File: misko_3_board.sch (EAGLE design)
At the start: 179 parts, among them IC1 ATMEGA1281-16AU, IC10 ORG1510-MK4, IC11 TPS3808G33DBVT, IC12 LTC4425, IC13 RN-42, IC14 ADXL345, IC15 74HCT1G32, IC16 FM25W256-SOIC, IC17 MICROSD_SPI_MODE, IC18 FH12-30S-0.5SH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

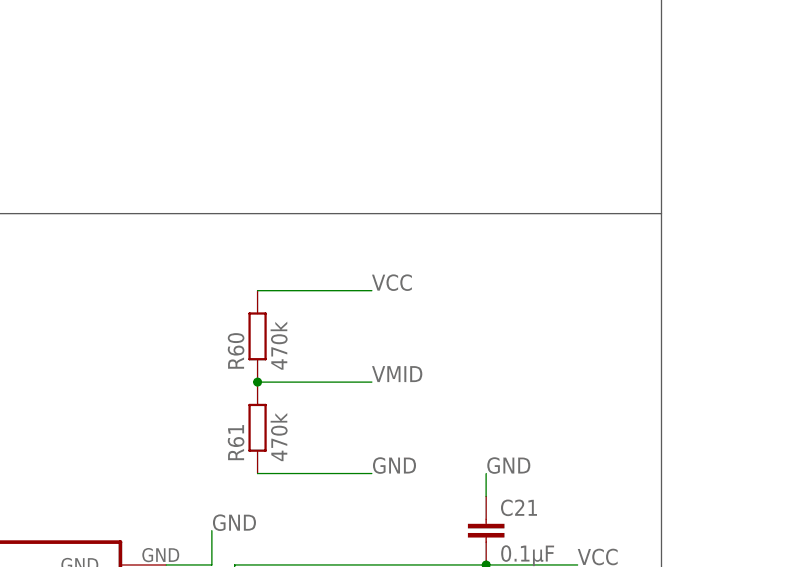
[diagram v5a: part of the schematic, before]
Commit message: - corrected resisitor divider for LTC4425 - R60/61 now connect to Vgps (instead of Vcc)
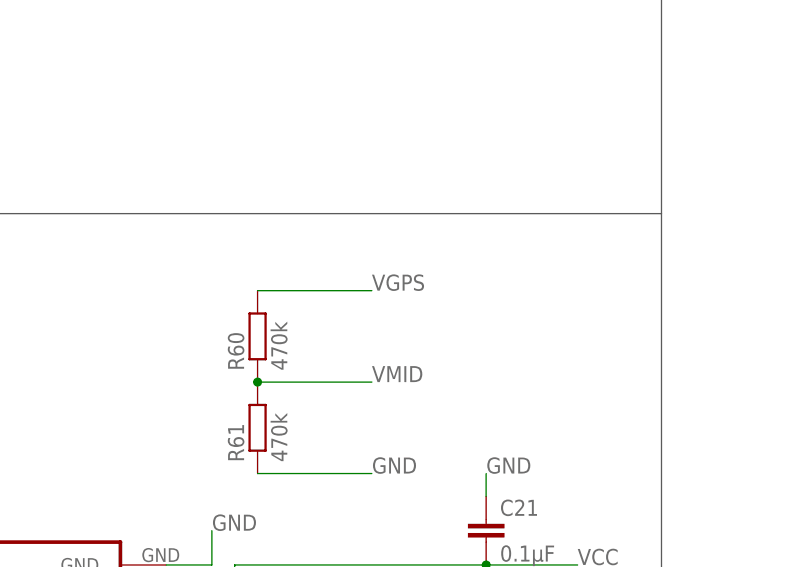
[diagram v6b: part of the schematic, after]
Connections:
- net VCC: no longer R60.2
- net VGPS: now also R60.2
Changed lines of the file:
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@@
 <label x="284.48" y="830.58" size="1.778" layer="95" ratio="9"/>
-</segment>
-<segment>
-<pinref part="R60" gate="G$1" pin="2"/>
-<wire x1="325.12" y1="93.98" x2="337.82" y2="93.98" width="0.1524" layer="91"/>
-<label x="337.82" y="93.98" size="1.778" layer="95"/>
 </segment>
 </net>
@@
 <junction x="279.4" y="60.96"/>
 </segment>
-</net>
+<segment>
+<pinref part="R60" gate="G$1" pin="2"/>
+<wire x1="325.12" y1="93.98" x2="337.82" y2="93.98" width="0.1524" layer="91"/>
+<label x="337.82" y="93.98" size="1.778" layer="95"/>
+</segment>
+</net>

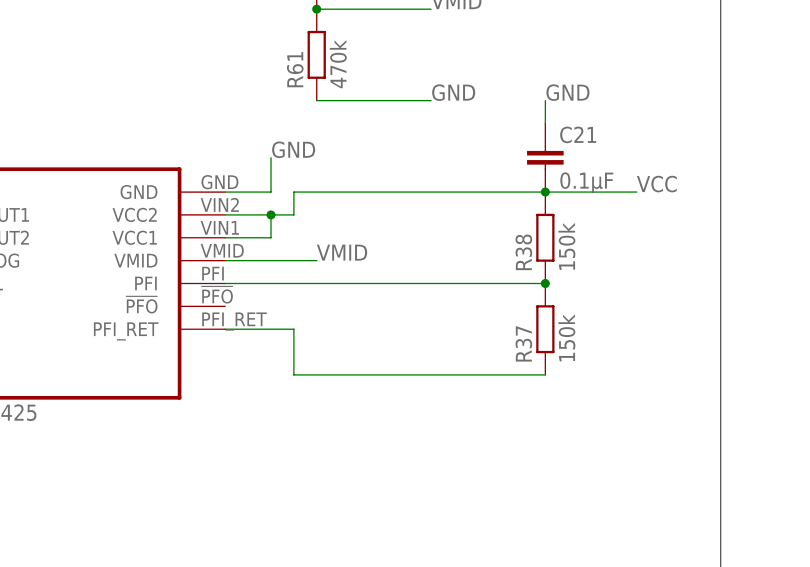
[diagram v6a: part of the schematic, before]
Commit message: - removed power fail functionality from LTC4425 since it is not needed at all
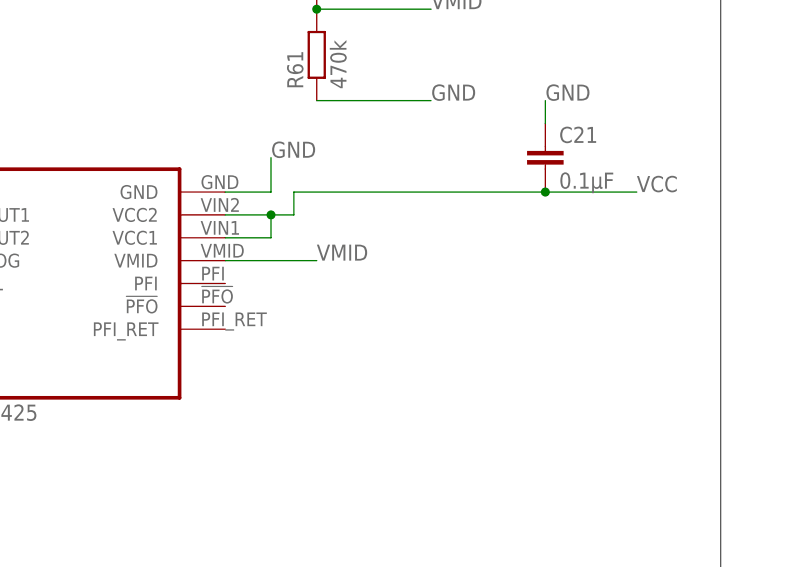
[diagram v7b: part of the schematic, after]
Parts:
- removed R37, R38: 150k, resistor:R-EU_R0805
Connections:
- removed net PFI: IC12.PFI, R37.2, R38.1
- removed net PFI_RET: IC12.PFI_RET, R37.1
- net VCC: no longer R38.2
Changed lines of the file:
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@@
 <part name="IC13" library="EN42-I Bluetooth Module" deviceset="RN-42" device=""/>
 <part name="IC12" library="LTC4425 Supercap Charger" deviceset="LTC4425" device=""/>
-<part name="R37" library="resistor" deviceset="R-EU_" device="R0805" value="150k"/>
-<part name="R38" library="resistor" deviceset="R-EU_" device="R0805" value="150k"/>
 <part name="R39" library="resistor" deviceset="R-EU_" device="R0805" value="1k"/>
 <part name="R40" library="resistor" deviceset="R-EU_" device="R0805" value="10k"/>
@@
 <instance part="IC13" gate="G$1" x="144.78" y="-35.56"/>
 <instance part="IC12" gate="G$1" x="297.18" y="53.34"/>
-<instance part="R37" gate="G$1" x="350.52" y="48.26" rot="R90"/>
-<instance part="R38" gate="G$1" x="350.52" y="58.42" rot="R90"/>
 <instance part="R39" gate="G$1" x="266.7" y="48.26"/>
 <instance part="R40" gate="G$1" x="269.24" y="55.88"/>
@@
 <junction x="320.04" y="60.96"/>
 <wire x1="322.58" y1="63.5" x2="350.52" y2="63.5" width="0.1524" layer="91"/>
-<pinref part="R38" gate="G$1" pin="2"/>
 <pinref part="C21" gate="G$1" pin="2"/>
 <junction x="350.52" y="63.5"/>
@@
 </segment>
 </net>
-<net name="PFI" class="2">
-<segment>
-<pinref part="R37" gate="G$1" pin="2"/>
-<pinref part="R38" gate="G$1" pin="1"/>
-<junction x="350.52" y="53.34"/>
-<wire x1="350.52" y1="53.34" x2="314.96" y2="53.34" width="0.1524" layer="91"/>
-<pinref part="IC12" gate="G$1" pin="PFI"/>
-</segment>
-</net>
 <net name="LTC4425_PROG" class="2">
 <segment>
@@
 </segment>
 </net>
-<net name="PFI_RET" class="2">
-<segment>
-<pinref part="R37" gate="G$1" pin="1"/>
-<wire x1="350.52" y1="43.18" x2="322.58" y2="43.18" width="0.1524" layer="91"/>
-<wire x1="322.58" y1="43.18" x2="322.58" y2="48.26" width="0.1524" layer="91"/>
-<pinref part="IC12" gate="G$1" pin="PFI_RET"/>
-<wire x1="322.58" y1="48.26" x2="314.96" y2="48.26" width="0.1524" layer="91"/>
-</segment>
-</net>
